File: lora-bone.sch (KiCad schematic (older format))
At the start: 16 parts, among them J1 Analog IN, J10 GS2, J11 GS2, J12 GS2, J13 GS2, J15 CONN_COAXIAL, J2 POWER, J3 Bluepill left, J4 PWM OUT, J5 SPI OUT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

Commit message: A few little corrections
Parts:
- renumbered J15 to ANT
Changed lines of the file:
@@
 DIO2
 $Comp
-L CONN_COAXIAL J15
+L CONN_COAXIAL ANT
 U 1 1 59AB09FA
 P 10500 2000
-F 0 "J15" H 10510 2120 50  0000 C CNN
+F 0 "ANT" H 10510 2120 50  0000 C CNN
 F 1 "CONN_COAXIAL" V 10615 2000 50  0000 C CNN
 F 2 "Connect:SMA_THT_Jack_Straight" H 10500 2000 50  0001 C CNN

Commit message: A few changes and corrections
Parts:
- U1: symbol RFM95W -> RFM95W-RESCUE-lora-bone
- renumbered ANT to ANT1
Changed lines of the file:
@@
 EESchema Schematic File Version 2
+LIBS:lora-bone-rescue
 LIBS:power
 LIBS:device
@@
 $EndDescr
 $Comp
-L RFM95W U1
+L RFM95W-RESCUE-lora-bone U1
 U 1 1 59AAFD06
 P 9450 1650
@@
 DIO2
 $Comp
-L CONN_COAXIAL ANT
+L CONN_COAXIAL ANT1
 U 1 1 59AB09FA
 P 10500 2000
-F 0 "ANT" H 10510 2120 50  0000 C CNN
+F 0 "ANT1" H 10510 2120 50  0000 C CNN
 F 1 "CONN_COAXIAL" V 10615 2000 50  0000 C CNN
 F 2 "Connect:SMA_THT_Jack_Straight" H 10500 2000 50  0001 C CNN

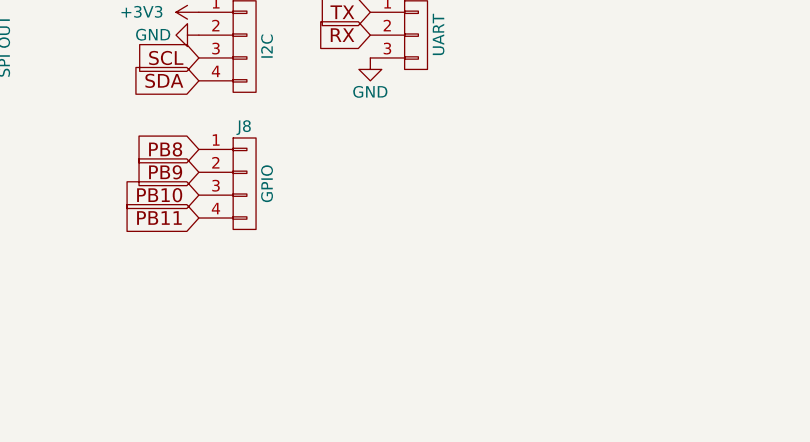
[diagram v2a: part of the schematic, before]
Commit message: Add power GPIO hint
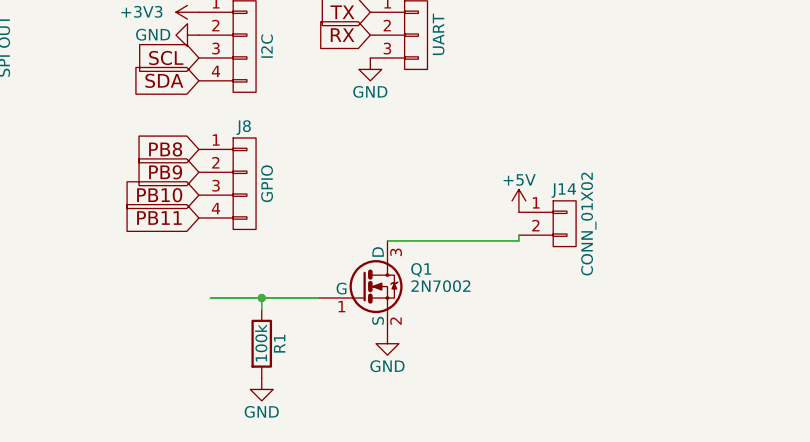
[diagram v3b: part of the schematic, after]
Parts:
- added J14: CONN_01X02, Pin_Headers:Pin_Header_Straight_1x02_Pitch2.54mm, symbol CONN_01X02
- added Q1: 2N7002, TO_SOT_Packages_SMD:SOT-23, symbol 2N7002
- added R1: 100k, Resistors_SMD:R_0805, symbol R
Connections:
- wire segments 1 -> 5
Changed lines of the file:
@@
 	1    0    0    -1
 $EndComp
+$Comp
+L 2N7002 Q1
+U 1 1 59AD954F
+P 5325 5200
+F 0 "Q1" H 5525 5275 50  0000 L CNN
+F 1 "2N7002" H 5525 5200 50  0000 L CNN
+F 2 "TO_SOT_Packages_SMD:SOT-23" H 5525 5125 50  0001 L CIN
+F 3 "" H 5325 5200 50  0001 L CNN
+	1    5325 5200
+	1    0    0    -1
+$EndComp
+$Comp
+L R R1
+U 1 1 59AD96AE
+P 4875 5450
+F 0 "R1" V 4955 5450 50  0000 C CNN
+F 1 "100k" V 4875 5450 50  0000 C CNN
+F 2 "Resistors_SMD:R_0805" V 4805 5450 50  0001 C CNN
+F 3 "" H 4875 5450 50  0001 C CNN
+	1    4875 5450
+	1    0    0    -1
+$EndComp
+$Comp
+L GND #PWR022
+U 1 1 59AD9719
+P 5425 5400
+F 0 "#PWR022" H 5425 5150 50  0001 C CNN
+F 1 "GND" H 5425 5250 50  0000 C CNN
+F 2 "" H 5425 5400 50  0001 C CNN
+F 3 "" H 5425 5400 50  0001 C CNN
+	1    5425 5400
+	1    0    0    -1
+$EndComp
+$Comp
+L GND #PWR023
+U 1 1 59AD9751
+P 4875 5600
+F 0 "#PWR023" H 4875 5350 50  0001 C CNN
+F 1 "GND" H 4875 5450 50  0000 C CNN
+F 2 "" H 4875 5600 50  0001 C CNN
+F 3 "" H 4875 5600 50  0001 C CNN
+	1    4875 5600
+	1    0    0    -1
+$EndComp
+Wire Wire Line
+	4875 5300 4875 5250
+Wire Wire Line
+	4650 5250 5125 5250
+Connection ~ 4875 5250
+Wire Wire Line
+	5425 5000 6000 5000
+$Comp
+L +5V #PWR024
+U 1 1 59ADBCD1
+P 6000 4875
+F 0 "#PWR024" H 6000 4725 50  0001 C CNN
+F 1 "+5V" H 6000 5015 50  0000 C CNN
+F 2 "" H 6000 4875 50  0001 C CNN
+F 3 "" H 6000 4875 50  0001 C CNN
+	1    6000 4875
+	1    0    0    -1
+$EndComp
+$Comp
+L CONN_01X02 J14
+U 1 1 59ADBD1B
+P 6200 4925
+F 0 "J14" H 6200 5075 50  0000 C CNN
+F 1 "CONN_01X02" V 6300 4925 50  0000 C CNN
+F 2 "Pin_Headers:Pin_Header_Straight_1x02_Pitch2.54mm" H 6200 4925 50  0001 C CNN
+F 3 "" H 6200 4925 50  0001 C CNN
+	1    6200 4925
+	1    0    0    -1
+$EndComp
+Wire Wire Line
+	6000 5000 6000 4975
 $EndSCHEMATC

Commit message: Power GPIO routet. Added Pull UP Resistor for PB8
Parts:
- added R2: 5k, Resistors_SMD:R_0805_HandSoldering, symbol R
- J14: value CONN_01X02 -> POWER OUT
- Q1: footprint TO_SOT_Packages_SMD:SOT-23 -> TO_SOT_Packages_SMD:SOT-23_Handsoldering
- R1: footprint Resistors_SMD:R_0805 -> Resistors_SMD:R_0805_HandSoldering
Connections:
- net labels added: PB12
- no-connect marks 8 -> 7
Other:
- moved on the sheet: J14, J8, Q1, R1
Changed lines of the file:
@@
 PA8
 Text GLabel 6200 2350 0    60   Input ~ 0
-PA8
+PB12
 $Comp
 L CONN_01X04 J8
 U 1 1 59AB4B50
-P 4800 4750
-F 0 "J8" H 4800 5000 50  0000 C CNN
-F 1 "GPIO" V 4900 4750 50  0000 C CNN
-F 2 "Pin_Headers:Pin_Header_Straight_1x04_Pitch2.54mm" H 4800 4750 50  0001 C CNN
-F 3 "" H 4800 4750 50  0001 C CNN
-	1    4800 4750
+P 4800 4800
+F 0 "J8" H 4800 5050 50  0000 C CNN
+F 1 "GPIO" V 4900 4800 50  0000 C CNN
+F 2 "Pin_Headers:Pin_Header_Straight_1x04_Pitch2.54mm" H 4800 4800 50  0001 C CNN
+F 3 "" H 4800 4800 50  0001 C CNN
+	1    4800 4800
 	1    0    0    -1
 $EndComp
@@
 NoConn ~ 2950 2650
 NoConn ~ 2950 2950
-NoConn ~ 3950 3250
-Text GLabel 4600 4600 0    60   Input ~ 0
+Text GLabel 4600 4650 0    60   Input ~ 0
 PB8
-Text GLabel 4600 4700 0    60   Input ~ 0
+Text GLabel 4600 4750 0    60   Input ~ 0
 PB9
-Text GLabel 4600 4800 0    60   Input ~ 0
+Text GLabel 4600 4850 0    60   Input ~ 0
 PB10
-Text GLabel 4600 4900 0    60   Input ~ 0
+Text GLabel 4600 4950 0    60   Input ~ 0
 PB11
 $Comp
@@
 L 2N7002 Q1
 U 1 1 59AD954F
-P 5325 5200
-F 0 "Q1" H 5525 5275 50  0000 L CNN
-F 1 "2N7002" H 5525 5200 50  0000 L CNN
-F 2 "TO_SOT_Packages_SMD:SOT-23" H 5525 5125 50  0001 L CIN
-F 3 "" H 5325 5200 50  0001 L CNN
-	1    5325 5200
+P 8675 4900
+F 0 "Q1" H 8875 4975 50  0000 L CNN
+F 1 "2N7002" H 8875 4900 50  0000 L CNN
+F 2 "TO_SOT_Packages_SMD:SOT-23_Handsoldering" H 8875 4825 50  0001 L CIN
+F 3 "" H 8675 4900 50  0001 L CNN
+	1    8675 4900
 	1    0    0    -1
 $EndComp
@@
 L R R1
 U 1 1 59AD96AE
-P 4875 5450
-F 0 "R1" V 4955 5450 50  0000 C CNN
-F 1 "100k" V 4875 5450 50  0000 C CNN
-F 2 "Resistors_SMD:R_0805" V 4805 5450 50  0001 C CNN
-F 3 "" H 4875 5450 50  0001 C CNN
-	1    4875 5450
+P 8225 5150
+F 0 "R1" V 8305 5150 50  0000 C CNN
+F 1 "100k" V 8225 5150 50  0000 C CNN
+F 2 "Resistors_SMD:R_0805_HandSoldering" V 8155 5150 50  0001 C CNN
+F 3 "" H 8225 5150 50  0001 C CNN
+	1    8225 5150
 	1    0    0    -1
 $EndComp
@@
 L GND #PWR022
 U 1 1 59AD9719
-P 5425 5400
-F 0 "#PWR022" H 5425 5150 50  0001 C CNN
-F 1 "GND" H 5425 5250 50  0000 C CNN
-F 2 "" H 5425 5400 50  0001 C CNN
-F 3 "" H 5425 5400 50  0001 C CNN
-	1    5425 5400
+P 8775 5100
+F 0 "#PWR022" H 8775 4850 50  0001 C CNN
+F 1 "GND" H 8775 4950 50  0000 C CNN
+F 2 "" H 8775 5100 50  0001 C CNN
+F 3 "" H 8775 5100 50  0001 C CNN
+	1    8775 5100
 	1    0    0    -1
 $EndComp
@@
 L GND #PWR023
 U 1 1 59AD9751
-P 4875 5600
-F 0 "#PWR023" H 4875 5350 50  0001 C CNN
-F 1 "GND" H 4875 5450 50  0000 C CNN
-F 2 "" H 4875 5600 50  0001 C CNN
-F 3 "" H 4875 5600 50  0001 C CNN
-	1    4875 5600
+P 8225 5300
+F 0 "#PWR023" H 8225 5050 50  0001 C CNN
+F 1 "GND" H 8225 5150 50  0000 C CNN
+F 2 "" H 8225 5300 50  0001 C CNN
+F 3 "" H 8225 5300 50  0001 C CNN
+	1    8225 5300
 	1    0    0    -1
 $EndComp
 Wire Wire Line
-	4875 5300 4875 5250
+	8225 5000 8225 4950
 Wire Wire Line
-	4650 5250 5125 5250
-Connection ~ 4875 5250
+	8000 4950 8475 4950
+Connection ~ 8225 4950
 Wire Wire Line
-	5425 5000 6000 5000
+	8775 4700 9350 4700
 $Comp
 L +5V #PWR024
 U 1 1 59ADBCD1
-P 6000 4875
-F 0 "#PWR024" H 6000 4725 50  0001 C CNN
-F 1 "+5V" H 6000 5015 50  0000 C CNN
-F 2 "" H 6000 4875 50  0001 C CNN
-F 3 "" H 6000 4875 50  0001 C CNN
-	1    6000 4875
+P 9350 4575
+F 0 "#PWR024" H 9350 4425 50  0001 C CNN
+F 1 "+5V" H 9350 4715 50  0000 C CNN
+F 2 "" H 9350 4575 50  0001 C CNN
+F 3 "" H 9350 4575 50  0001 C CNN
+	1    9350 4575
 	1    0    0    -1
 $EndComp
@@
 L CONN_01X02 J14
 U 1 1 59ADBD1B
-P 6200 4925
-F 0 "J14" H 6200 5075 50  0000 C CNN
-F 1 "CONN_01X02" V 6300 4925 50  0000 C CNN
-F 2 "Pin_Headers:Pin_Header_Straight_1x02_Pitch2.54mm" H 6200 4925 50  0001 C CNN
-F 3 "" H 6200 4925 50  0001 C CNN
-	1    6200 4925
+P 9550 4625
+F 0 "J14" H 9550 4775 50  0000 C CNN
+F 1 "POWER OUT" V 9650 4625 50  0000 C CNN
+F 2 "Pin_Headers:Pin_Header_Straight_1x02_Pitch2.54mm" H 9550 4625 50  0001 C CNN
+F 3 "" H 9550 4625 50  0001 C CNN
+	1    9550 4625
 	1    0    0    -1
 $EndComp
 Wire Wire Line
-	6000 5000 6000 4975
+	9350 4700 9350 4675
+Text GLabel 3950 3250 2    60   Input ~ 0
+PB12
+Text GLabel 8000 4950 0    60   Input ~ 0
+PA8
+$Comp
+L R R2
+U 1 1 59ADA338
+P 7400 3475
+F 0 "R2" V 7480 3475 50  0000 C CNN
+F 1 "5k" V 7400 3475 50  0000 C CNN
+F 2 "Resistors_SMD:R_0805_HandSoldering" V 7330 3475 50  0001 C CNN
+F 3 "" H 7400 3475 50  0001 C CNN
+	1    7400 3475
+	1    0    0    -1
+$EndComp
+$Comp
+L +5V #PWR025
+U 1 1 59ADA43C
+P 7400 3325
+F 0 "#PWR025" H 7400 3175 50  0001 C CNN
+F 1 "+5V" H 7400 3465 50  0000 C CNN
+F 2 "" H 7400 3325 50  0001 C CNN
+F 3 "" H 7400 3325 50  0001 C CNN
+	1    7400 3325
+	1    0    0    -1
+$EndComp
+Text GLabel 7400 3625 3    60   Input ~ 0
+PB8
 $EndSCHEMATC

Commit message: Added Pull Ups for I2C.
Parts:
- added R3, R4: 5k, Resistors_SMD:R_0805_HandSoldering, symbol R
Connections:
- net +3V3: now also R3.1, R4.1
- net SCL: now also R3.2
- net SDA: now also R4.2
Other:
- moved on the sheet: R2
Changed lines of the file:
@@
 L R R2
 U 1 1 59ADA338
-P 7400 3475
-F 0 "R2" V 7480 3475 50  0000 C CNN
-F 1 "5k" V 7400 3475 50  0000 C CNN
-F 2 "Resistors_SMD:R_0805_HandSoldering" V 7330 3475 50  0001 C CNN
-F 3 "" H 7400 3475 50  0001 C CNN
-	1    7400 3475
+P 7650 3475
+F 0 "R2" V 7730 3475 50  0000 C CNN
+F 1 "5k" V 7650 3475 50  0000 C CNN
+F 2 "Resistors_SMD:R_0805_HandSoldering" V 7580 3475 50  0001 C CNN
+F 3 "" H 7650 3475 50  0001 C CNN
+	1    7650 3475
 	1    0    0    -1
 $EndComp
@@
 L +5V #PWR025
 U 1 1 59ADA43C
-P 7400 3325
-F 0 "#PWR025" H 7400 3175 50  0001 C CNN
-F 1 "+5V" H 7400 3465 50  0000 C CNN
-F 2 "" H 7400 3325 50  0001 C CNN
-F 3 "" H 7400 3325 50  0001 C CNN
-	1    7400 3325
+P 7650 3325
+F 0 "#PWR025" H 7650 3175 50  0001 C CNN
+F 1 "+5V" H 7650 3465 50  0000 C CNN
+F 2 "" H 7650 3325 50  0001 C CNN
+F 3 "" H 7650 3325 50  0001 C CNN
+	1    7650 3325
 	1    0    0    -1
 $EndComp
-Text GLabel 7400 3625 3    60   Input ~ 0
+Text GLabel 7650 3625 3    60   Input ~ 0
 PB8
+$Comp
+L R R3
+U 1 1 59ADB7C4
+P 7900 3475
+F 0 "R3" V 7980 3475 50  0000 C CNN
+F 1 "5k" V 7900 3475 50  0000 C CNN
+F 2 "Resistors_SMD:R_0805_HandSoldering" V 7830 3475 50  0001 C CNN
+F 3 "" H 7900 3475 50  0001 C CNN
+	1    7900 3475
+	1    0    0    -1
+$EndComp
+Text GLabel 7900 3625 3    60   Input ~ 0
+SCL
+$Comp
+L R R4
+U 1 1 59ADB849
+P 8100 3475
+F 0 "R4" V 8180 3475 50  0000 C CNN
+F 1 "5k" V 8100 3475 50  0000 C CNN
+F 2 "Resistors_SMD:R_0805_HandSoldering" V 8030 3475 50  0001 C CNN
+F 3 "" H 8100 3475 50  0001 C CNN
+	1    8100 3475
+	1    0    0    -1
+$EndComp
+Text GLabel 8100 3625 3    60   Input ~ 0
+SDA
+$Comp
+L +3V3 #PWR026
+U 1 1 59ADB907
+P 7900 3325
+F 0 "#PWR026" H 7900 3175 50  0001 C CNN
+F 1 "+3V3" H 7900 3465 50  0000 C CNN
+F 2 "" H 7900 3325 50  0001 C CNN
+F 3 "" H 7900 3325 50  0001 C CNN
+	1    7900 3325
+	1    0    0    -1
+$EndComp
+$Comp
+L +3V3 #PWR027
+U 1 1 59ADB9B5
+P 8100 3325
+F 0 "#PWR027" H 8100 3175 50  0001 C CNN
+F 1 "+3V3" H 8100 3465 50  0000 C CNN
+F 2 "" H 8100 3325 50  0001 C CNN
+F 3 "" H 8100 3325 50  0001 C CNN
+	1    8100 3325
+	1    0    0    -1
+$EndComp
 $EndSCHEMATC
